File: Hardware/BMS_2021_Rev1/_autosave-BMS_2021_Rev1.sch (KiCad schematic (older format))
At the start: 11 parts

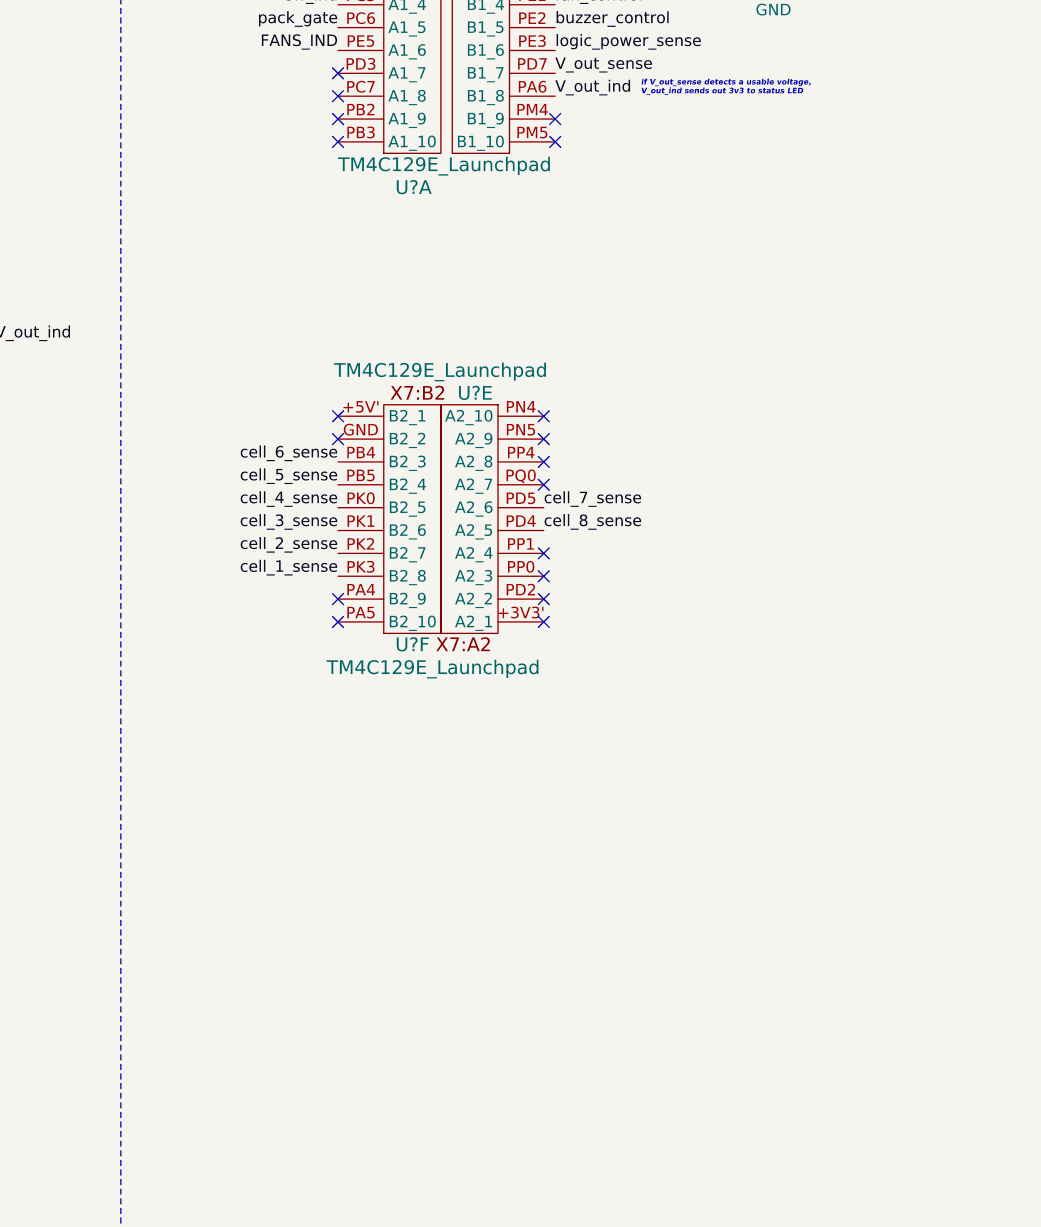
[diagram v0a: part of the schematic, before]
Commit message: stuff added
-cellFilter IC and R values added
-MOSFET values added
-extra TIVA headers added
-currentSense R values labeled properly
-things are actually connected together this time
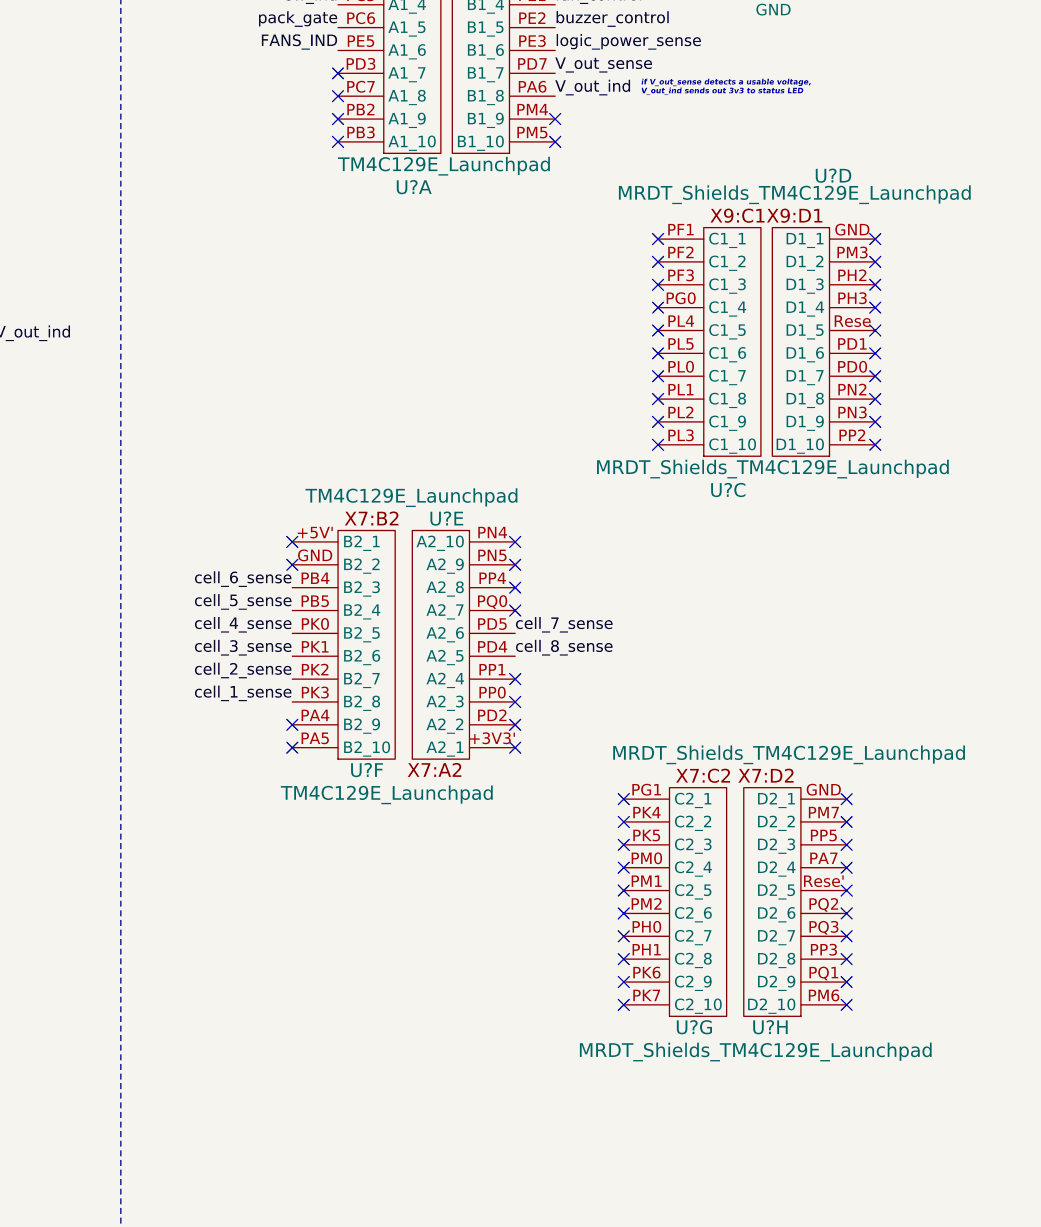
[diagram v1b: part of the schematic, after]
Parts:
- added U? (x4): MRDT_Shields_TM4C129E_Launchpad, symbol BMS_2021_Rev1-cache:MRDT_Shields_TM4C129E_Launchpad
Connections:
- no-connect marks 19 -> 59
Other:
- moved on the sheet: U?E, U?F
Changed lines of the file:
@@
-$Comp
-L MRDT_Shields:TM4C129E_Launchpad U?
-U 6 1 5F7FD340
-P 7800 3950
-F 0 "U?" H 7850 3900 60  0000 L CNN
-F 1 "TM4C129E_Launchpad" H 7550 3800 60  0000 L CNN
-F 2 "" H 7800 3950 60  0001 C CNN
-F 3 "" H 7800 3950 60  0001 C CNN
-	6    7800 3950
-	1    0    0    -1
-$EndComp
-$Comp
-L MRDT_Shields:TM4C129E_Launchpad U?
-U 5 1 5F805ECA
-P 8300 2950
-F 0 "U?" H 8400 2900 60  0000 C CNN
-F 1 "TM4C129E_Launchpad" H 8550 2800 60  0000 C CNN
-F 2 "" H 8300 2950 60  0001 C CNN
-F 3 "" H 8300 2950 60  0001 C CNN
-	5    8300 2950
-	-1   0    0    1
-$EndComp
 $Comp
 L MRDT_Shields:TM4C129E_Launchpad U?
@@
 NoConn ~ 8550 1800
 NoConn ~ 8550 1700
-NoConn ~ 7600 3000
-NoConn ~ 7600 3100
-NoConn ~ 7600 3900
-NoConn ~ 7600 3800
-NoConn ~ 8500 3900
-NoConn ~ 8500 3800
-NoConn ~ 8500 3700
-NoConn ~ 8500 3600
-NoConn ~ 8500 3300
-NoConn ~ 8500 3200
-NoConn ~ 8500 3100
-NoConn ~ 8500 3000
+NoConn ~ 7400 3550
+NoConn ~ 7400 3650
+NoConn ~ 7400 4450
+NoConn ~ 7400 4350
 Wire Wire Line
 	3800 2625 3950 2625
@@
 Text Label 4900 3300 2    50   ~ 0
 sw_ind
-Text Label 7600 3700 2    50   ~ 0
+Text Label 7400 4250 2    50   ~ 0
 cell_1_sense
-Text Label 7600 3600 2    50   ~ 0
+Text Label 7400 4150 2    50   ~ 0
 cell_2_sense
-Text Label 7600 3500 2    50   ~ 0
+Text Label 7400 4050 2    50   ~ 0
 cell_3_sense
-Text Label 7600 3400 2    50   ~ 0
+Text Label 7400 3950 2    50   ~ 0
 cell_4_sense
-Text Label 7600 3300 2    50   ~ 0
+Text Label 7400 3850 2    50   ~ 0
 cell_5_sense
-Text Label 7600 3200 2    50   ~ 0
+Text Label 7400 3750 2    50   ~ 0
 cell_6_sense
-Text Label 8500 3400 0    50   ~ 0
-cell_7_sense
-Text Label 8500 3500 0    50   ~ 0
-cell_8_sense
 NoConn ~ 8550 900
 Wire Wire Line
@@
 	1    0    0    -1
 $EndComp
+$Comp
+L BMS_2021_Rev1-cache:MRDT_Shields_TM4C129E_Launchpad U?
+U 3 1 5FA5E750
+P 9200 3175
+F 0 "U?" H 9225 3025 60  0000 L CNN
+F 1 "MRDT_Shields_TM4C129E_Launchpad" H 8725 3125 60  0000 L CNN
+F 2 "" H 9200 3175 60  0001 C CNN
+F 3 "" H 9200 3175 60  0001 C CNN
+	3    9200 3175
+	1    0    0    -1
+$EndComp
+$Comp
+L BMS_2021_Rev1-cache:MRDT_Shields_TM4C129E_Launchpad U?
+U 4 1 5FA60370
+P 9750 3175
+F 0 "U?" H 9650 4400 60  0000 L CNN
+F 1 "MRDT_Shields_TM4C129E_Launchpad" H 9125 4325 60  0000 L CNN
+F 2 "" H 9750 3175 60  0001 C CNN
+F 3 "" H 9750 3175 60  0001 C CNN
+	4    9750 3175
+	-1   0    0    -1
+$EndComp
+Text Label 8375 4050 0    50   ~ 0
+cell_8_sense
+Text Label 8375 3950 0    50   ~ 0
+cell_7_sense
+NoConn ~ 8375 3550
+NoConn ~ 8375 3650
+NoConn ~ 8375 3750
+NoConn ~ 8375 3850
+NoConn ~ 8375 4150
+NoConn ~ 8375 4250
+NoConn ~ 8375 4350
+NoConn ~ 8375 4450
+$Comp
+L MRDT_Shields:TM4C129E_Launchpad U?
+U 5 1 5F805ECA
+P 8175 3500
+F 0 "U?" H 8275 3450 60  0000 C CNN
+F 1 "TM4C129E_Launchpad" H 8425 3350 60  0000 C CNN
+F 2 "" H 8175 3500 60  0001 C CNN
+F 3 "" H 8175 3500 60  0001 C CNN
+	5    8175 3500
+	-1   0    0    1
+$EndComp
+$Comp
+L MRDT_Shields:TM4C129E_Launchpad U?
+U 6 1 5F7FD340
+P 7600 4500
+F 0 "U?" H 7650 4450 60  0000 L CNN
+F 1 "TM4C129E_Launchpad" H 7350 4350 60  0000 L CNN
+F 2 "" H 7600 4500 60  0001 C CNN
+F 3 "" H 7600 4500 60  0001 C CNN
+	6    7600 4500
+	1    0    0    -1
+$EndComp
+$Comp
+L BMS_2021_Rev1-cache:MRDT_Shields_TM4C129E_Launchpad U?
+U 7 1 5FA7F4A6
+P 9050 5625
+F 0 "U?" H 9075 5575 60  0000 L CNN
+F 1 "MRDT_Shields_TM4C129E_Launchpad" H 8650 5475 60  0000 L CNN
+F 2 "" H 9050 5625 60  0001 C CNN
+F 3 "" H 9050 5625 60  0001 C CNN
+	7    9050 5625
+	1    0    0    -1
+$EndComp
+$Comp
+L BMS_2021_Rev1-cache:MRDT_Shields_TM4C129E_Launchpad U?
+U 8 1 5FA81FAC
+P 9625 5625
+F 0 "U?" H 9675 5575 60  0000 L CNN
+F 1 "MRDT_Shields_TM4C129E_Launchpad" H 8900 6775 60  0000 L CNN
+F 2 "" H 9625 5625 60  0001 C CNN
+F 3 "" H 9625 5625 60  0001 C CNN
+	8    9625 5625
+	-1   0    0    -1
+$EndComp
+NoConn ~ 9825 4675
+NoConn ~ 9825 4775
+NoConn ~ 9825 4875
+NoConn ~ 9825 4975
+NoConn ~ 9825 5075
+NoConn ~ 9825 5175
+NoConn ~ 9825 5275
+NoConn ~ 9825 5375
+NoConn ~ 9825 5475
+NoConn ~ 9825 5575
+NoConn ~ 8850 5575
+NoConn ~ 8850 5475
+NoConn ~ 8850 5375
+NoConn ~ 8850 5275
+NoConn ~ 8850 5175
+NoConn ~ 8850 5075
+NoConn ~ 8850 4975
+NoConn ~ 8850 4875
+NoConn ~ 8850 4775
+NoConn ~ 8850 4675
+NoConn ~ 9950 2225
+NoConn ~ 9950 2325
+NoConn ~ 9950 2425
+NoConn ~ 9950 2525
+NoConn ~ 9950 2625
+NoConn ~ 9950 2725
+NoConn ~ 9950 2825
+NoConn ~ 9950 2925
+NoConn ~ 9950 3025
+NoConn ~ 9950 3125
+NoConn ~ 9000 3125
+NoConn ~ 9000 3025
+NoConn ~ 9000 2925
+NoConn ~ 9000 2825
+NoConn ~ 9000 2725
+NoConn ~ 9000 2625
+NoConn ~ 9000 2525
+NoConn ~ 9000 2425
+NoConn ~ 9000 2325
+NoConn ~ 9000 2225
 $EndSCHEMATC
